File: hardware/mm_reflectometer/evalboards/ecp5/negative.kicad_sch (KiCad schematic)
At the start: 18 parts, among them U701 LM2776, U702 TPS72301DB

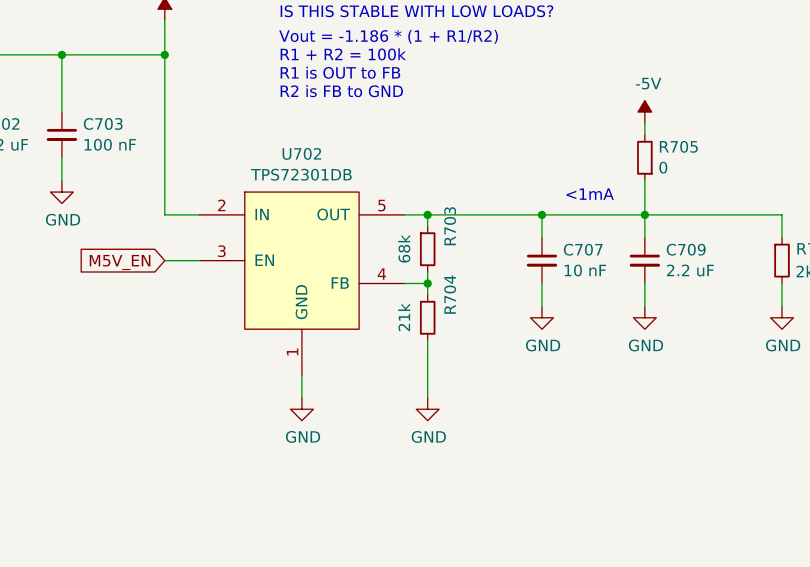
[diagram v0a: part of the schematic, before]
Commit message: cleanup ecp5 schematic, generated assembly drawings
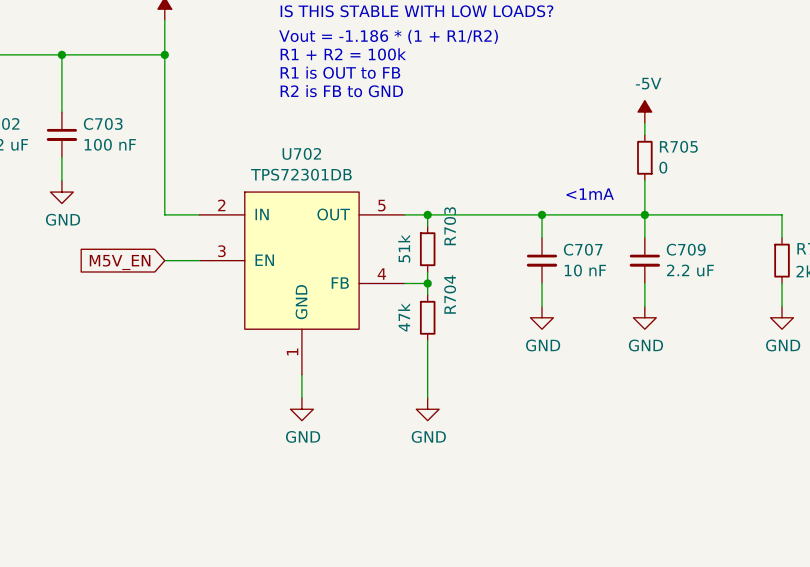
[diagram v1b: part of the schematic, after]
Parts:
- R703: value 68k -> 51k
- R704: value 21k -> 47k
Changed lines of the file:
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@@
     (in_bom yes) (on_board yes)
     (property "Reference" "R703" (id 0) (at 118.11 92.71 90))
-    (property "Value" "68k" (id 1) (at 113.03 95.25 90))
+    (property "Value" "51k" (id 1) (at 113.03 95.25 90))
     (property "Footprint" "Resistor_SMD:R_0402_1005Metric" (id 2) (at 115.57 95.25 0)
       (effects (font (size 1.27 1.27)) hide)
@@
     (in_bom yes) (on_board yes)
     (property "Reference" "R704" (id 0) (at 118.11 100.33 90))
-    (property "Value" "21k" (id 1) (at 113.03 102.87 90))
+    (property "Value" "47k" (id 1) (at 113.03 102.87 90))
     (property "Footprint" "Resistor_SMD:R_0402_1005Metric" (id 2) (at 115.57 102.87 0)
       (effects (font (size 1.27 1.27)) hide)
